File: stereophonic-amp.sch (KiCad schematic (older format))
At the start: 53 parts

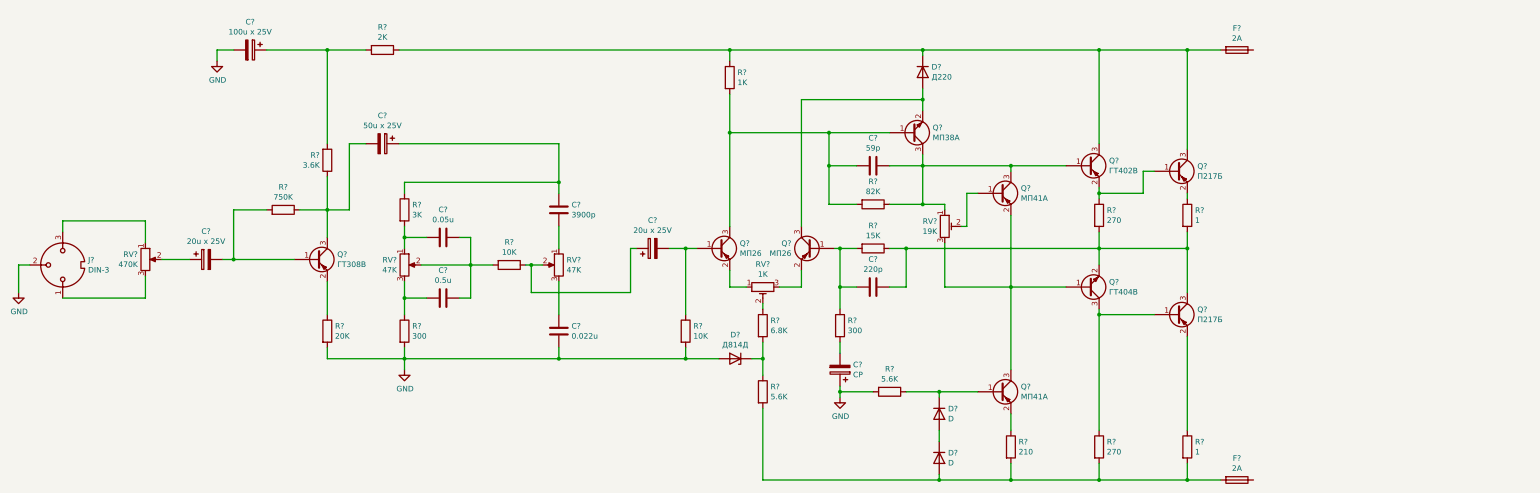
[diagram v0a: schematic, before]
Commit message: Finish schematic
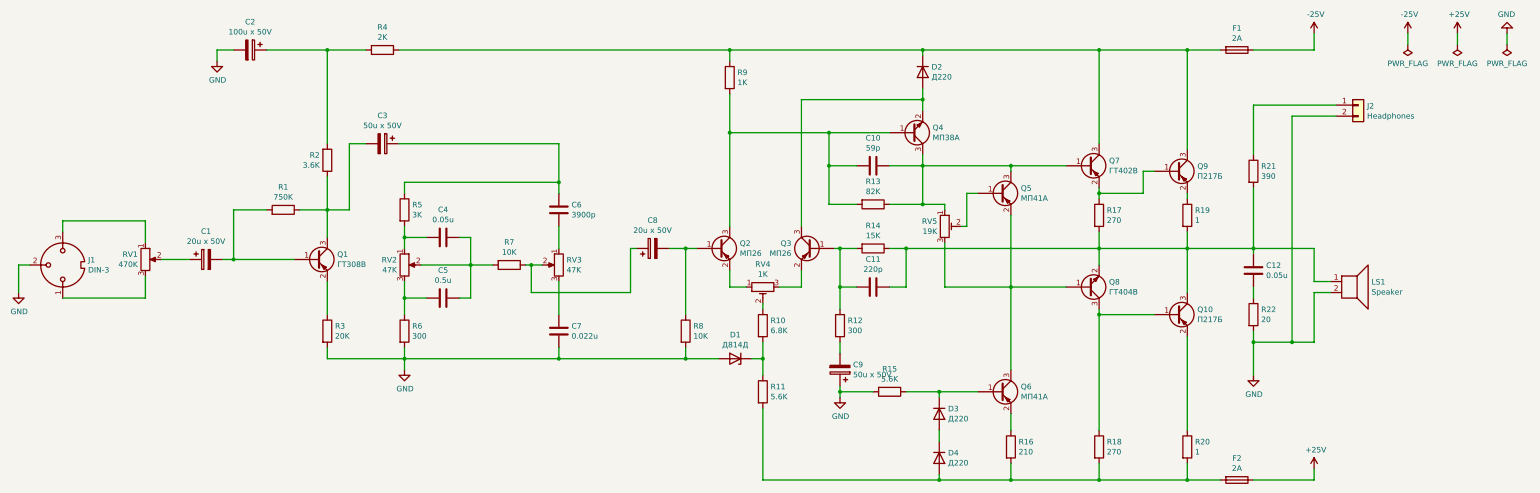
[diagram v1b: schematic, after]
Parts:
- added C12: 0.05u, Capacitor_THT:C_Rect_L4.6mm_W3.8mm_P2.50mm_MKS02_FKP02, symbol Device:C
- added J2: Headphones, Connector_PinHeader_2.54mm:PinHeader_1x02_P2.54mm_Vertical, symbol Connector_Generic:Conn_01x02
- added LS1: Speaker, Connector_PinHeader_2.54mm:PinHeader_1x02_P2.54mm_Vertical, symbol Device:Speaker
- added R21: 390, Resistor_THT:R_Axial_DIN0207_L6.3mm_D2.5mm_P10.16mm_Horizontal, symbol Device:R
- added R22: 20, Resistor_THT:R_Axial_DIN0309_L9.0mm_D3.2mm_P12.70mm_Horizontal, symbol Device:R
- C1, C8: renamed from C?; value 20u x 25V -> 20u x 50V; footprint (none) -> Capacitor_THT:CP_Radial_D5.0mm_P2.00mm
- C10, C11, C5: renamed from C?; footprint (none) -> Capacitor_THT:C_Rect_L7.0mm_W4.5mm_P5.00mm
- C2: renamed from C?; value 100u x 25V -> 100u x 50V; footprint (none) -> Capacitor_THT:CP_Radial_D6.3mm_P2.50mm
- C3: renamed from C?; value 50u x 25V -> 50u x 50V; footprint (none) -> Capacitor_THT:CP_Radial_D6.3mm_P2.50mm
- C4, C6, C7: renamed from C?; footprint (none) -> Capacitor_THT:C_Rect_L4.6mm_W3.8mm_P2.50mm_MKS02_FKP02
- C9: renamed from C?; value CP -> 50u x 50V; footprint (none) -> Capacitor_THT:CP_Radial_D6.3mm_P2.50mm
- D1: renamed from D?; footprint (none) -> Diode_THT:D_DO-15_P15.24mm_Horizontal
- D2: renamed from D?; footprint (none) -> Diode_THT:D_A-405_P12.70mm_Horizontal
- D3, D4: renamed from D?; value D -> Д220; footprint (none) -> Diode_THT:D_A-405_P12.70mm_Horizontal
- F1, F2: renamed from F?; footprint (none) -> Fuse:Fuseholder_Cylinder-5x20mm_Stelvio-Kontek_PTF78_Horizontal_Open
- J1: renamed from J?; footprint (none) -> Connector_PinHeader_2.54mm:PinHeader_1x03_P2.54mm_Vertical
- Q1: renamed from Q?; footprint (none) -> stereophonic-amp:TO-11-3
- Q10, Q6, Q9: renamed from Q?; footprint (none) -> Connector_PinHeader_1.00mm:PinHeader_1x03_P1.00mm_Vertical
- Q2, Q3, Q4, Q5, Q7, Q8: renamed from Q?; footprint (none) -> Package_TO_SOT_THT:TO-11-3
- R1, R10, R11, R12, R13, R14, R15, R16, R17, R18, R2, R3, R4, R5, R6, R7, R8, R9: renamed from R?; footprint (none) -> Resistor_THT:R_Axial_DIN0207_L6.3mm_D2.5mm_P10.16mm_Horizontal
- R19, R20: renamed from R?; footprint (none) -> Resistor_THT:R_Axial_DIN0414_L11.9mm_D4.5mm_P20.32mm_Horizontal
- RV1, RV2, RV3: renamed from RV?; footprint (none) -> Connector_PinHeader_2.54mm:PinHeader_1x03_P2.54mm_Vertical
- RV4, RV5: renamed from RV?; footprint (none) -> Potentiometer_THT:Potentiometer_Piher_PT-15-V15_Vertical
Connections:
- net GND: now also J2.2 (Pin_2), LS1.2, R22.2
- net at C11.1, Q10.3 (C), Q8.2 (E)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: now also C12.1, LS1.1, R21.2
- net -25V: now reaches F1.1
- net +25V: now reaches F2.1
- new net: J2.1 (Pin_1), R21.1
- new net: C12.2, R22.1
